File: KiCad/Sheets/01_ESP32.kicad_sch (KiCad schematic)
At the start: 1 part, among them U1 ESP32-DEVKITC-32UE

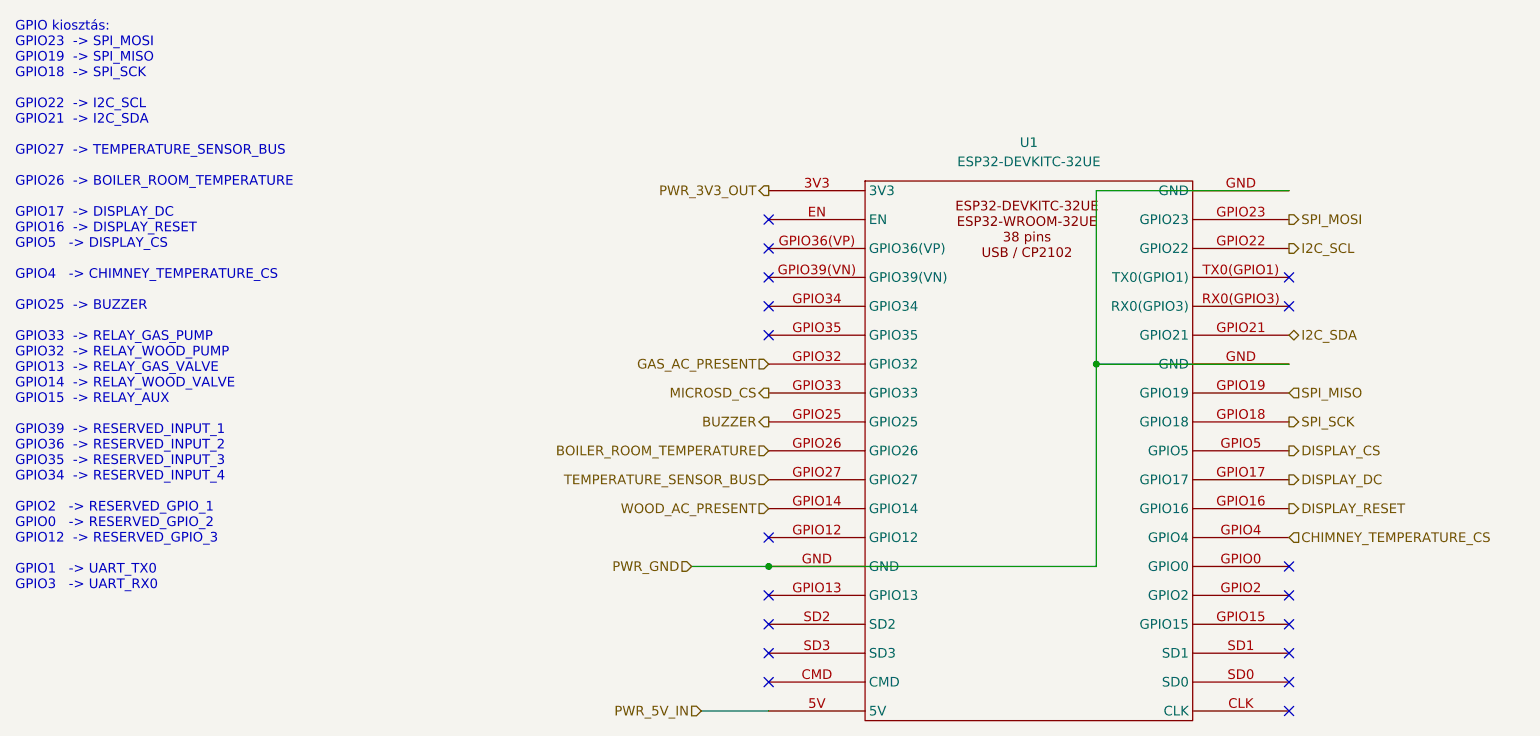
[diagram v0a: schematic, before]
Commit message: LEDs sheet added, schematic finished
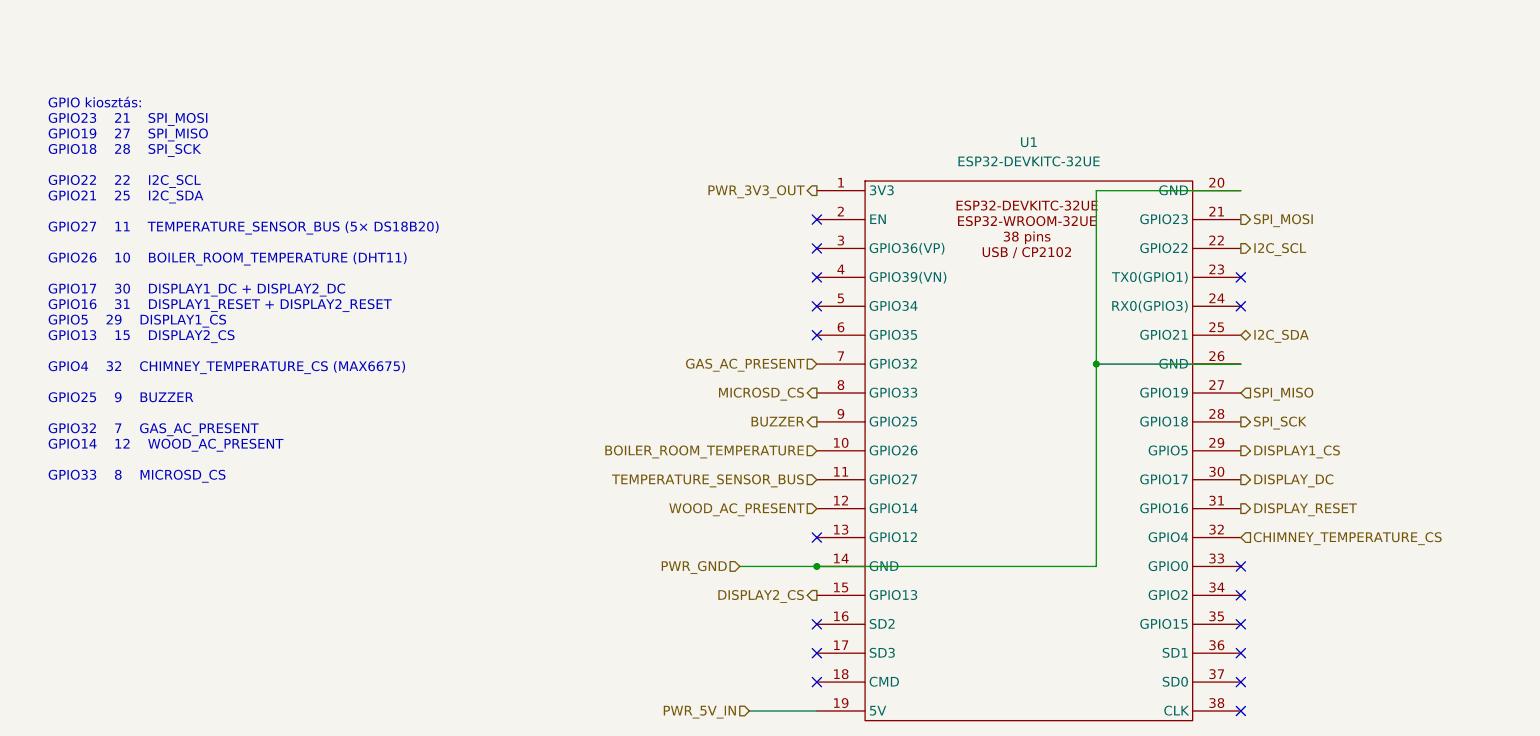
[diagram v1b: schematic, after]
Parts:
- U1: footprint (none) -> HMS_Footprints:ESP32_DEVKITC_32UE
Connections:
- net BOILER_ROOM_TEMPERATURE: now also U1.10 (GPIO26); no longer U1.GPIO26
- net BUZZER: now also U1.9 (GPIO25); no longer U1.GPIO25
- net CHIMNEY_TEMPERATURE_CS: now also U1.32 (GPIO4); no longer U1.GPIO4
- net DISPLAY_DC: now also U1.30 (GPIO17); no longer U1.GPIO17
- net DISPLAY_RESET: now also U1.31 (GPIO16); no longer U1.GPIO16
- net GAS_AC_PRESENT: now also U1.7 (GPIO32); no longer U1.GPIO32
- net I2C_SCL: now also U1.22 (GPIO22); no longer U1.GPIO22
- net I2C_SDA: now also U1.25 (GPIO21); no longer U1.GPIO21
- net MICROSD_CS: now also U1.8 (GPIO33); no longer U1.GPIO33
- net PWR_3V3_OUT: now also U1.1 (3V3); no longer U1.3V3
- net PWR_5V_IN: now also U1.19 (5V); no longer U1.5V
- net PWR_GND: now also U1.14 (GND), U1.20 (GND), U1.26 (GND); no longer U1.GND
- net SPI_MISO: now also U1.27 (GPIO19); no longer U1.GPIO19
- net SPI_MOSI: now also U1.21 (GPIO23); no longer U1.GPIO23
- net SPI_SCK: now also U1.28 (GPIO18); no longer U1.GPIO18
- net TEMPERATURE_SENSOR_BUS: now also U1.11 (GPIO27); no longer U1.GPIO27
- net WOOD_AC_PRESENT: now also U1.12 (GPIO14); no longer U1.GPIO14
- removed net DISPLAY_CS: U1.GPIO5
- new net DISPLAY1_CS: U1.29 (GPIO5)
- new net DISPLAY2_CS: U1.15 (GPIO13)
- no-connect marks 18 -> 17
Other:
- note added: "GPIO kiosztás: GPIO23 21 SPI_MOSI GPIO19 27 SPI_MISO GPIO18 28 SPI_SCK GPIO22 22 I2C_SCL GPIO21 25 I2C_SDA GPIO27 11 TEMPERATURE_SENSOR_BUS (5× DS18B20) GPIO26 10 BOILER_ROOM_TEMPERATURE (DHT11) GPIO17 30 DISPLAY1_DC + DISPLAY2_DC GPIO16 31 DISPLAY1_RESET + DISPLAY2_RESET GPIO5 29 DISPLAY1_CS GPIO13 15 DISPLAY2_CS GPIO4 32 CHIMNEY_TEMPERATURE_CS (MAX6675) GPIO25 9 BUZZER GPIO32 7 GAS_AC_PRESENT G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"
- note removed: "GPIO kiosztás: GPIO23 -> SPI_MOSI GPIO19 -> SPI_MISO GPIO18 -> SPI_SCK GPIO22 -> I2C_SCL GPIO21 -> I2C_SDA GPIO27 -> TEMPERATURE_SENSOR_BUS GPIO26 -> BOILER_ROOM_TEMPERATURE GPIO17 -> DISPLAY_DC GPIO16 -> DISPLAY_RESET GPIO5 -> DISPLAY_CS GPIO4 -> CHIMNEY_TEMPERATURE_CS GPIO25 -> BUZZER GPIO33 -> RELAY_GAS_PUMP GPIO32 -> RELAY_WOOD_PUMP GPIO13 -> RELAY_GAS_VALVE GPIO14 -> RELAY_WOOD_VALVE GPIO15 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"
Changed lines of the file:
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@@
 		(comment 3 "ESP32 DevKit")
 	)
-	(text "GPIO kiosztás:\nGPIO23  -> SPI_MOSI\nGPIO19  -> SPI_MISO\nGPIO18  -> SPI_SCK\n\nGPIO22  -> I2C_SCL\nGPIO21  -> I2C_SDA\n\nGPIO27  -> TEMPERATURE_SENSOR_BUS\n\nGPIO26  -> BOILER_ROOM_TEMPERATURE\n\nGPIO17  -> DISPLAY_DC\nGPIO16  -> DISPLAY_RESET\nGPIO5   -> DISPLAY_CS\n\nGPIO4   -> CHIMNEY_TEMPERATURE_CS\n\nGPIO25  -> BUZZER\n\nGPIO33  -> RELAY_GAS_PUMP\nGPIO32  -> RELAY_WOOD_PUMP\nGPIO13  -> RELAY_GAS_VALVE\nGPIO14  -> RELAY_WOOD_VALVE\nGPIO15  -> RELAY_AUX\n\nGPIO39  -> RESERVED_INPUT_1\nGPIO36  -> RESERVED_INPUT_2\nGPIO35  -> RESERVED_INPUT_3\nGPIO34  -> RESERVED_INPUT_4\n\nGPIO2   -> RESERVED_GPIO_1\nGPIO0   -> RESERVED_GPIO_2\nGPIO12  -> RESERVED_GPIO_3\n\nGPIO1   -> UART_TX0\nGPIO3   -> UART_RX0"
+	(text "GPIO kiosztás:\nGPIO23	21	SPI_MOSI\nGPIO19	27	SPI_MISO\nGPIO18	28	SPI_SCK\n\nGPIO22	22	I2C_SCL\nGPIO21	25	I2C_SDA\n\nGPIO27	11	TEMPERATURE_SENSOR_BUS (5× DS18B20)\n\nGPIO26	10	BOILER_ROOM_TEMPERATURE (DHT11)\n\nGPIO17	30	DISPLAY1_DC + DISPLAY2_DC\nGPIO16	31	DISPLAY1_RESET + DISPLAY2_RESET\nGPIO5	29	DISPLAY1_CS\nGPIO13	15	DISPLAY2_CS\n\nGPIO4	32	CHIMNEY_TEMPERATURE_CS (MAX6675)\n\nGPIO25	9	BUZZER\n\nGPIO32	7	GAS_AC_PRESENT\nGPIO14	12	WOOD_AC_PRESENT\n\nGPIO33	8	MICROSD_CS"
 		(exclude_from_sim no)
-		(at 16.256 53.34 0)
+		(at 20.574 51.308 0)
 		(effects
 			(font
@@
 	)
 	(junction
-		(at 115.57 87.63)
+		(at 121.92 87.63)
 		(diameter 0)
 		(color 0 0 0 1)
 	)
 	(no_connect
-		(at 115.57 45.72)
-	)
-	(no_connect
-		(at 184.15 49.53)
-	)
-	(no_connect
-		(at 115.57 91.44)
-	)
-	(no_connect
-		(at 184.15 53.34)
-	)
-	(no_connect
-		(at 115.57 83.82)
-	)
-	(no_connect
-		(at 115.57 99.06)
-	)
-	(no_connect
-		(at 115.57 49.53)
-	)
-	(no_connect
-		(at 115.57 41.91)
-	)
-	(no_connect
-		(at 115.57 57.15)
-	)
-	(no_connect
-		(at 184.15 91.44)
-	)
-	(no_connect
-		(at 115.57 102.87)
-	)
-	(no_connect
-		(at 184.15 87.63)
-	)
-	(no_connect
-		(at 184.15 102.87)
-	)
-	(no_connect
-		(at 115.57 53.34)
-	)
-	(no_connect
-		(at 184.15 99.06)
-	)
-	(no_connect
-		(at 115.57 95.25)
-	)
-	(no_connect
-		(at 184.15 106.68)
-	)
-	(no_connect
-		(at 184.15 95.25)
+		(at 121.92 45.72)
+	)
+	(no_connect
+		(at 177.8 49.53)
+	)
+	(no_connect
+		(at 177.8 53.34)
+	)
+	(no_connect
+		(at 121.92 83.82)
+	)
+	(no_connect
+		(at 121.92 99.06)
+	)
+	(no_connect
+		(at 121.92 49.53)
+	)
+	(no_connect
+		(at 121.92 41.91)
+	)
+	(no_connect
+		(at 121.92 57.15)
+	)
+	(no_connect
+		(at 177.8 91.44)
+	)
+	(no_connect
+		(at 121.92 102.87)
+	)
+	(no_connect
+		(at 177.8 87.63)
+	)
+	(no_connect
+		(at 177.8 102.87)
+	)
+	(no_connect
+		(at 121.92 53.34)
+	)
+	(no_connect
+		(at 177.8 99.06)
+	)
+	(no_connect
+		(at 121.92 95.25)
+	)
+	(no_connect
+		(at 177.8 106.68)
+	)
+	(no_connect
+		(at 177.8 95.25)
 	)
 	(wire
@@
 	(wire
 		(pts
-			(xy 158.75 60.96) (xy 184.15 60.96)
+			(xy 158.75 60.96) (xy 177.8 60.96)
 		)
 		(stroke
@@
 	(wire
 		(pts
-			(xy 184.15 38.1) (xy 158.75 38.1)
+			(xy 177.8 38.1) (xy 158.75 38.1)
 		)
 		(stroke
@@
 	(wire
 		(pts
-			(xy 106.68 106.68) (xy 115.57 106.68)
+			(xy 113.03 106.68) (xy 121.92 106.68)
 		)
 		(stroke
@@
 	(wire
 		(pts
-			(xy 105.41 87.63) (xy 115.57 87.63)
+			(xy 111.76 87.63) (xy 121.92 87.63)
 		)
 		(stroke
@@
 	(wire
 		(pts
-			(xy 115.57 87.63) (xy 158.75 87.63)
+			(xy 121.92 87.63) (xy 158.75 87.63)
 		)
 		(stroke
@@
 	(hierarchical_label "DISPLAY_RESET"
 		(shape output)
-		(at 184.15 80.01 0)
+		(at 177.8 80.01 0)
 		(effects
 			(font
@@
 	(hierarchical_label "CHIMNEY_TEMPERATURE_CS"
 		(shape input)
-		(at 184.15 83.82 0)
+		(at 177.8 83.82 0)
 		(effects
 			(font
@@
 	(hierarchical_label "SPI_SCK"
 		(shape output)
-		(at 184.15 68.58 0)
-		(effects
-			(font
-				(size 1.27 1.27)
-			)
-			(justify left)
-		)
-	)
-	(hierarchical_label "DISPLAY_CS"
-		(shape output)
-		(at 184.15 72.39 0)
-		(effects
-			(font
-				(size 1.27 1.27)
-			)
-			(justify left)
+		(at 177.8 68.58 0)
+		(effects
+			(font
+				(size 1.27 1.27)
+			)
+			(justify left)
+		)
+	)
+	(hierarchical_label "DISPLAY1_CS"
+		(shape output)
+		(at 177.8 72.39 0)
+		(effects
+			(font
+				(size 1.27 1.27)
+			)
+			(justify left)
+		)
+	)
+	(hierarchical_label "DISPLAY2_CS"
+		(shape output)
+		(at 121.92 91.44 180)
+		(effects
+			(font
+				(size 1.27 1.27)
+			)
+			(justify right)
 		)
 	)
 	(hierarchical_label "I2C_SDA"
 		(shape bidirectional)
-		(at 184.15 57.15 0)
+		(at 177.8 57.15 0)
 		(effects
 			(font
@@
 	(hierarchical_label "BUZZER"
 		(shape output)
-		(at 115.57 68.58 180)
+		(at 121.92 68.58 180)
 		(effects
 			(font
@@
 	(hierarchical_label "PWR_3V3_OUT"
 		(shape output)
-		(at 115.57 38.1 180)
+		(at 121.92 38.1 180)
 		(effects
 			(font
@@
 	(hierarchical_label "TEMPERATURE_SENSOR_BUS"
 		(shape input)
-		(at 115.57 76.2 180)
+		(at 121.92 76.2 180)
 		(effects
 			(font
@@
 	(hierarchical_label "PWR_5V_IN"
 		(shape input)
-		(at 106.68 106.68 180)
+		(at 113.03 106.68 180)
 		(effects
 			(font
@@
 	(hierarchical_label "BOILER_ROOM_TEMPERATURE"
 		(shape input)
-		(at 115.57 72.39 180)
+		(at 121.92 72.39 180)
 		(effects
 			(font
@@
 	(hierarchical_label "PWR_GND"
 		(shape input)
-		(at 105.41 87.63 180)
+		(at 111.76 87.63 180)
 		(effects
 			(font
@@
 	(hierarchical_label "SPI_MISO"
 		(shape input)
-		(at 184.15 64.77 0)
+		(at 177.8 64.77 0)
 		(effects
 			(font
@@
 	(hierarchical_label "DISPLAY_DC"
 		(shape output)
-		(at 184.15 76.2 0)
+		(at 177.8 76.2 0)
 		(effects
 			(font
@@
 	(hierarchical_label "SPI_MOSI"
 		(shape output)
-		(at 184.15 41.91 0)
+		(at 177.8 41.91 0)
 		(effects
 			(font
@@
 	(hierarchical_label "MICROSD_CS"
 		(shape output)
-		(at 115.57 64.77 180)
+		(at 121.92 64.77 180)
 		(effects
 			(font
@@
 	(hierarchical_label "WOOD_AC_PRESENT"
 		(shape input)
-		(at 115.57 80.01 180)
+		(at 121.92 80.01 180)
 		(effects
 			(font
@@
 	(hierarchical_label "GAS_AC_PRESENT"
 		(shape input)
-		(at 115.57 60.96 180)
+		(at 121.92 60.96 180)
 		(effects
 			(font
@@
 	(hierarchical_label "I2C_SCL"
 		(shape output)
-		(at 184.15 45.72 0)
+		(at 177.8 45.72 0)
 		(effects
 			(font
@@
 			)
 		)
-		(property "Footprint" ""
+		(property "Footprint" "HMS_Footprints:ESP32_DEVKITC_32UE"
 			(at 134.62 34.29 0)
 			(hide yes)
@@
 			)
 		)
-		(pin "GPIO12"
-		)
-		(pin "GPIO17"
-		)
-		(pin "GPIO5"
-		)
-		(pin "GPIO13"
-		)
-		(pin "GPIO14"
-		)
-		(pin "GPIO15"
-		)
-		(pin "GPIO16"
-		)
-		(pin "GPIO32"
-		)
-		(pin "GPIO22"
-		)
-		(pin "GPIO39(VN)"
-		)
-		(pin "GPIO27"
-		)
-		(pin "GPIO21"
-		)
-		(pin "GPIO18"
-		)
-		(pin "GPIO26"
-		)
-		(pin "GPIO23"
-		)
-		(pin "GPIO34"
-		)
-		(pin "GPIO35"
-		)
-		(pin "SD1"
-		)
-		(pin "SD2"
-		)
-		(pin "GPIO19"
-		)
-		(pin "GPIO33"
-		)
-		(pin "SD0"
-		)
-		(pin "SD3"
-		)
-		(pin "GPIO25"
-		)
-		(pin "GPIO36(VP)"
-		)
-		(pin "TX0(GPIO1)"
-		)
-		(pin "RX0(GPIO3)"
-		)
-		(pin "CLK"
-		)
-		(pin "EN"
-		)
-		(pin "GPIO4"
-		)
-		(pin "5V"
-		)
-		(pin "GND"
-		)
-		(pin "GPIO0"
-		)
-		(pin "3V3"
-		)
-		(pin "CMD"
-		)
-		(pin "GPIO2"
-		)
-		(pin "GND"
-		)
-		(pin "GND"
+		(pin "31"
+		)
+		(pin "32"
+		)
+		(pin "38"
+		)
+		(pin "22"
+		)
+		(pin "20"
+		)
+		(pin "25"
+		)
+		(pin "34"
+		)
+		(pin "26"
+		)
+		(pin "23"
+		)
+		(pin "21"
+		)
+		(pin "7"
+		)
+		(pin "14"
+		)
+		(pin "35"
+		)
+		(pin "16"
+		)
+		(pin "29"
+		)
+		(pin "8"
+		)
+		(pin "9"
+		)
+		(pin "24"
+		)
+		(pin "36"
+		)
+		(pin "33"
+		)
+		(pin "17"
+		)
+		(pin "27"
+		)
+		(pin "28"
+		)
+		(pin "30"
+		)
+		(pin "37"
+		)
+		(pin "13"
+		)
+		(pin "12"
+		)
+		(pin "10"
+		)
+		(pin "11"
+		)
+		(pin "15"
+		)
+		(pin "19"
+		)
+		(pin "4"
+		)
+		(pin "18"
+		)
+		(pin "1"
+		)
+		(pin "6"
+		)
+		(pin "5"
+		)
+		(pin "3"
+		)
+		(pin "2"
 		)
 		(instances

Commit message: Finished PCB
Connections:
- net CHIMNEY_TEMPERATURE_CS: now also U1.12 (GPIO14); no longer U1.32 (GPIO4)
- net DISPLAY2_CS: now also U1.32 (GPIO4); no longer U1.15 (GPIO13)
- net MICROSD_CS: now also U1.15 (GPIO13); no longer U1.8 (GPIO33)
- net WOOD_AC_PRESENT: now also U1.8 (GPIO33); no longer U1.12 (GPIO14)
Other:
- note added: "GPIO kiosztás: GPIO23 SPI_MOSI GPIO19 SPI_MISO GPIO18 SPI_SCK GPIO22 I2C_SCL GPIO21 I2C_SDA GPIO27 TEMPERATURE_SENSOR_BUS (5× DS18B20) GPIO26 BOILER_ROOM_TEMPERATURE (DHT11) GPIO17 DISPLAY1_DC + DISPLAY2_DC GPIO16 DISPLAY1_RESET + DISPLAY2_RESET GPIO5 DISPLAY1_CS GPIO4 DISPLAY2_CS GPIO14 CHIMNEY_TEMPERATURE_CS (MAX6675) GPIO25 BUZZER GPIO32 GAS_AC_PRESENT GPIO33 WOOD_AC_PRESENT GPIO13 MICROSD_CS"
- note removed: "GPIO kiosztás: GPIO23 21 SPI_MOSI GPIO19 27 SPI_MISO GPIO18 28 SPI_SCK GPIO22 22 I2C_SCL GPIO21 25 I2C_SDA GPIO27 11 TEMPERATURE_SENSOR_BUS (5× DS18B20) GPIO26 10 BOILER_ROOM_TEMPERATURE (DHT11) GPIO17 30 DISPLAY1_DC + DISPLAY2_DC GPIO16 31 DISPLAY1_RESET + DISPLAY2_RESET GPIO5 29 DISPLAY1_CS GPIO13 15 DISPLAY2_CS GPIO4 32 CHIMNEY_TEMPERATURE_CS (MAX6675) GPIO25 9 BUZZER GPIO32 7 GAS_AC_PRESENT G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"
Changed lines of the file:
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@@
 		(comment 3 "ESP32 DevKit")
 	)
-	(text "GPIO kiosztás:\nGPIO23	21	SPI_MOSI\nGPIO19	27	SPI_MISO\nGPIO18	28	SPI_SCK\n\nGPIO22	22	I2C_SCL\nGPIO21	25	I2C_SDA\n\nGPIO27	11	TEMPERATURE_SENSOR_BUS (5× DS18B20)\n\nGPIO26	10	BOILER_ROOM_TEMPERATURE (DHT11)\n\nGPIO17	30	DISPLAY1_DC + DISPLAY2_DC\nGPIO16	31	DISPLAY1_RESET + DISPLAY2_RESET\nGPIO5	29	DISPLAY1_CS\nGPIO13	15	DISPLAY2_CS\n\nGPIO4	32	CHIMNEY_TEMPERATURE_CS (MAX6675)\n\nGPIO25	9	BUZZER\n\nGPIO32	7	GAS_AC_PRESENT\nGPIO14	12	WOOD_AC_PRESENT\n\nGPIO33	8	MICROSD_CS"
+	(text "GPIO kiosztás:\nGPIO23 SPI_MOSI\nGPIO19 SPI_MISO\nGPIO18 SPI_SCK\n\nGPIO22 I2C_SCL\nGPIO21 I2C_SDA\n\nGPIO27 TEMPERATURE_SENSOR_BUS (5× DS18B20)\n\nGPIO26 BOILER_ROOM_TEMPERATURE (DHT11)\n\nGPIO17 DISPLAY1_DC + DISPLAY2_DC\nGPIO16 DISPLAY1_RESET + DISPLAY2_RESET\nGPIO5  DISPLAY1_CS\nGPIO4  DISPLAY2_CS\n\nGPIO14 CHIMNEY_TEMPERATURE_CS (MAX6675)\n\nGPIO25 BUZZER\n\nGPIO32 GAS_AC_PRESENT\nGPIO33 WOOD_AC_PRESENT\n\nGPIO13 MICROSD_CS"
 		(exclude_from_sim no)
-		(at 20.574 51.308 0)
+		(at 21.59 48.006 0)
 		(effects
 			(font
@@
 	(hierarchical_label "CHIMNEY_TEMPERATURE_CS"
 		(shape input)
+		(at 121.92 80.01 180)
+		(effects
+			(font
+				(size 1.27 1.27)
+			)
+			(justify right)
+		)
+	)
+	(hierarchical_label "SPI_SCK"
+		(shape output)
+		(at 177.8 68.58 0)
+		(effects
+			(font
+				(size 1.27 1.27)
+			)
+			(justify left)
+		)
+	)
+	(hierarchical_label "DISPLAY1_CS"
+		(shape output)
+		(at 177.8 72.39 0)
+		(effects
+			(font
+				(size 1.27 1.27)
+			)
+			(justify left)
+		)
+	)
+	(hierarchical_label "DISPLAY2_CS"
+		(shape output)
 		(at 177.8 83.82 0)
 		(effects
@@
 			)
 			(justify left)
-		)
-	)
-	(hierarchical_label "SPI_SCK"
-		(shape output)
-		(at 177.8 68.58 0)
-		(effects
-			(font
-				(size 1.27 1.27)
-			)
-			(justify left)
-		)
-	)
-	(hierarchical_label "DISPLAY1_CS"
-		(shape output)
-		(at 177.8 72.39 0)
-		(effects
-			(font
-				(size 1.27 1.27)
-			)
-			(justify left)
-		)
-	)
-	(hierarchical_label "DISPLAY2_CS"
-		(shape output)
-		(at 121.92 91.44 180)
-		(effects
-			(font
-				(size 1.27 1.27)
-			)
-			(justify right)
 		)
 	)
@@
 	(hierarchical_label "MICROSD_CS"
 		(shape output)
+		(at 121.92 91.44 180)
+		(effects
+			(font
+				(size 1.27 1.27)
+			)
+			(justify right)
+		)
+	)
+	(hierarchical_label "WOOD_AC_PRESENT"
+		(shape input)
 		(at 121.92 64.77 180)
 		(effects
 			(font
-				(size 1.27 1.27)
-			)
-			(justify right)
-		)
-	)
-	(hierarchical_label "WOOD_AC_PRESENT"
-		(shape input)
-		(at 121.92 80.01 180)
-		(effects
-			(font
